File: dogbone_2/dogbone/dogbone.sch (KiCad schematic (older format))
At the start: 11 parts, among them J1 jstsh4x1, U1 TLV2771CDBVT

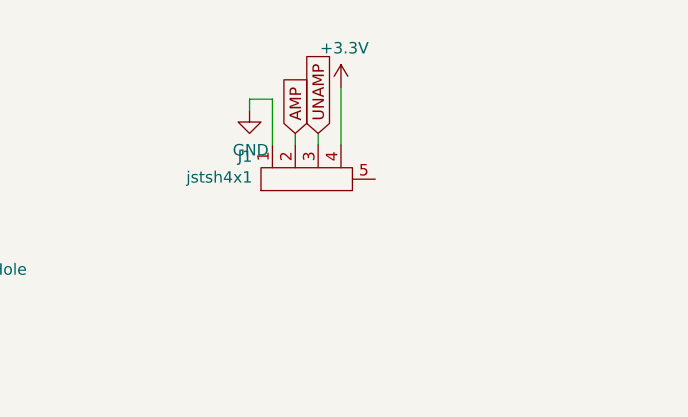
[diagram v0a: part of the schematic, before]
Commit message: updated dog bone schematic
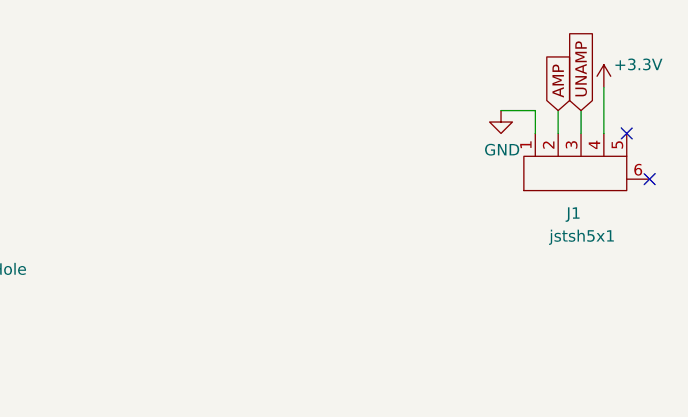
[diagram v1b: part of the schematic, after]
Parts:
- removed J1: jstsh4x1, exocam_charge_amp:jstsh4x1, symbol exocam_charge_amp:jstsh4x1
- added J1: jstsh5x1, symbol exocam_charge_amp:jstsh5x1
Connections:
- net +3V3: now also J1.4
- net AMP: now also J1.2
- net GND: now also J1.1
- net UNAMP: now also J1.3
- no-connect marks 0 -> 2
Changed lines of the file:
@@
 UNAMP
 $Comp
-L exocam_charge_amp:jstsh4x1 J1
-U 1 1 60E73D05
-P 4800 1050
-F 0 "J1" V 4849 1088 50  0000 L CNN
-F 1 "jstsh4x1" V 4758 1088 50  0000 L CNN
-F 2 "exocam_charge_amp:jstsh4x1" H 4750 1200 50  0001 C CNN
-F 3 "" H 4750 1200 50  0001 C CNN
-	1    4800 1050
+L exocam_charge_amp:jstsh5x1 J1
+U 1 1 60F6C4B2
+P 5950 1000
+F 0 "J1" V 5700 750 50  0000 L CNN
+F 1 "jstsh5x1" V 5600 600 50  0000 L CNN
+F 2 "" H 5900 1150 50  0001 C CNN
+F 3 "" H 5900 1150 50  0001 C CNN
+	1    5950 1000
 	0    -1   -1   0
 $EndComp
 $Comp
-L power:GND #PWR0105
-U 1 1 60E75791
-P 4750 800
-F 0 "#PWR0105" H 4750 550 50  0001 C CNN
-F 1 "GND" H 4755 627 50  0000 C CNN
-F 2 "" H 4750 800 50  0001 C CNN
-F 3 "" H 4750 800 50  0001 C CNN
-	1    4750 800
+L power:GND #PWR?
+U 1 1 60F6D49D
+P 5850 800
+F 0 "#PWR?" H 5850 550 50  0001 C CNN
+F 1 "GND" H 5855 627 50  0000 C CNN
+F 2 "" H 5850 800 50  0001 C CNN
+F 3 "" H 5850 800 50  0001 C CNN
+	1    5850 800
 	1    0    0    -1
 $EndComp
-Wire Wire Line
-	4750 750  4750 800
-Wire Wire Line
-	4750 750  4850 750
-Wire Wire Line
-	4850 750  4850 950
 $Comp
-L exocam_charge_amp-cache:+3.3V #PWR0106
-U 1 1 60E76333
-P 5150 700
-F 0 "#PWR0106" H 5150 550 50  0001 C CNN
-F 1 "+3.3V" H 5165 873 50  0000 C CNN
-F 2 "" H 5150 700 50  0001 C CNN
-F 3 "" H 5150 700 50  0001 C CNN
-	1    5150 700
+L exocam_charge_amp-cache:+3.3V #PWR?
+U 1 1 60F6DA28
+P 6300 700
+F 0 "#PWR?" H 6300 550 50  0001 C CNN
+F 1 "+3.3V" H 6450 800 50  0000 C CNN
+F 2 "" H 6300 700 50  0001 C CNN
+F 3 "" H 6300 700 50  0001 C CNN
+	1    6300 700
 	1    0    0    -1
 $EndComp
-Wire Wire Line
-	5150 700  5150 950
-Text GLabel 4950 900  1    50   Input ~ 0
+Text GLabel 6100 800  1    50   Input ~ 0
 AMP
-Text GLabel 5050 900  1    50   Input ~ 0
+Text GLabel 6200 800  1    50   Input ~ 0
 UNAMP
 Wire Wire Line
-	4950 900  4950 950
+	6300 900  6300 700
 Wire Wire Line
-	5050 900  5050 950
+	6200 900  6200 800
+Wire Wire Line
+	6100 900  6100 800
+Wire Wire Line
+	6000 900  6000 800
+Wire Wire Line
+	6000 800  5850 800
+NoConn ~ 6400 900
+NoConn ~ 6500 1100
 $EndSCHEMATC
